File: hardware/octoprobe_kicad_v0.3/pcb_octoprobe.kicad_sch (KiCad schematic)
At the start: 9 parts, among them J102 USB-226-BRW

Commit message: PCB: Oscillator
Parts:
- R104: footprint Resistor_SMD:R_0603_1608Metric -> Resistor_SMD:R_0805_2012Metric
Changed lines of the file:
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@@
 			)
 		)
-		(property "Footprint" "Resistor_SMD:R_0603_1608Metric"
+		(property "Footprint" "Resistor_SMD:R_0805_2012Metric"
 			(at 140.97 46.482 90)
 			(effects

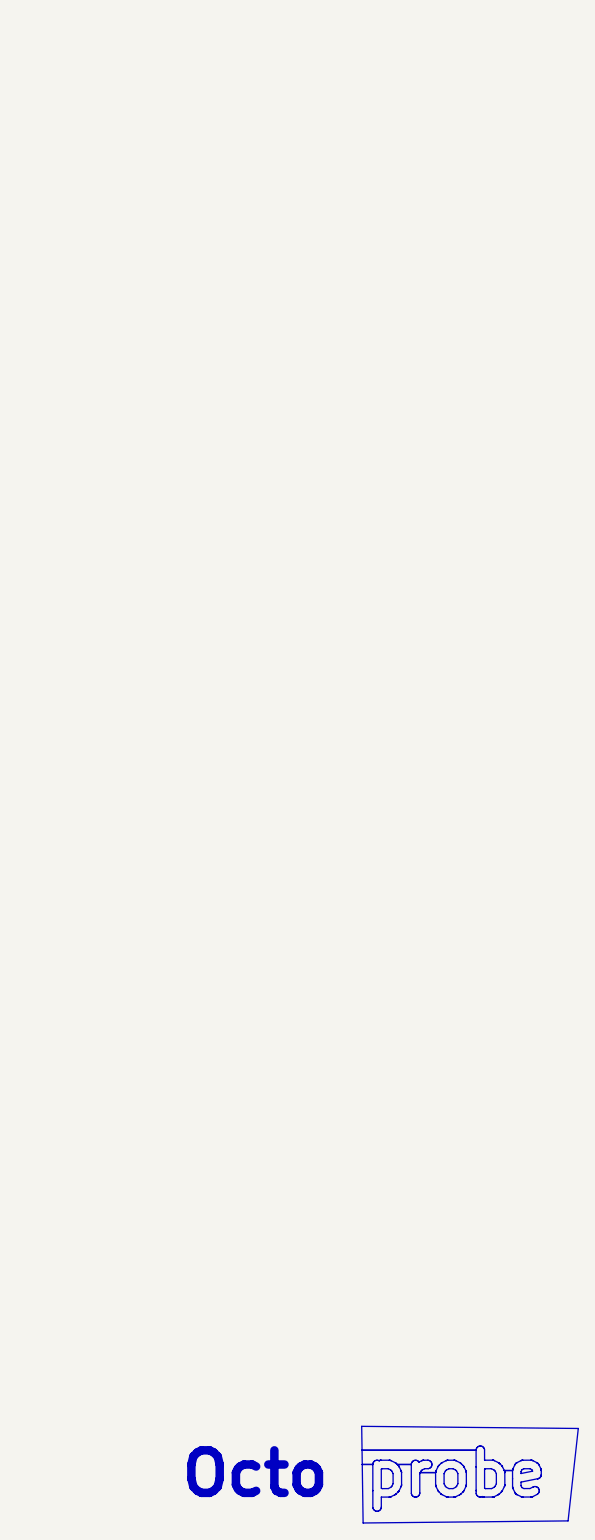
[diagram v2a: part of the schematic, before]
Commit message: PCB: Add "Open Hardware"
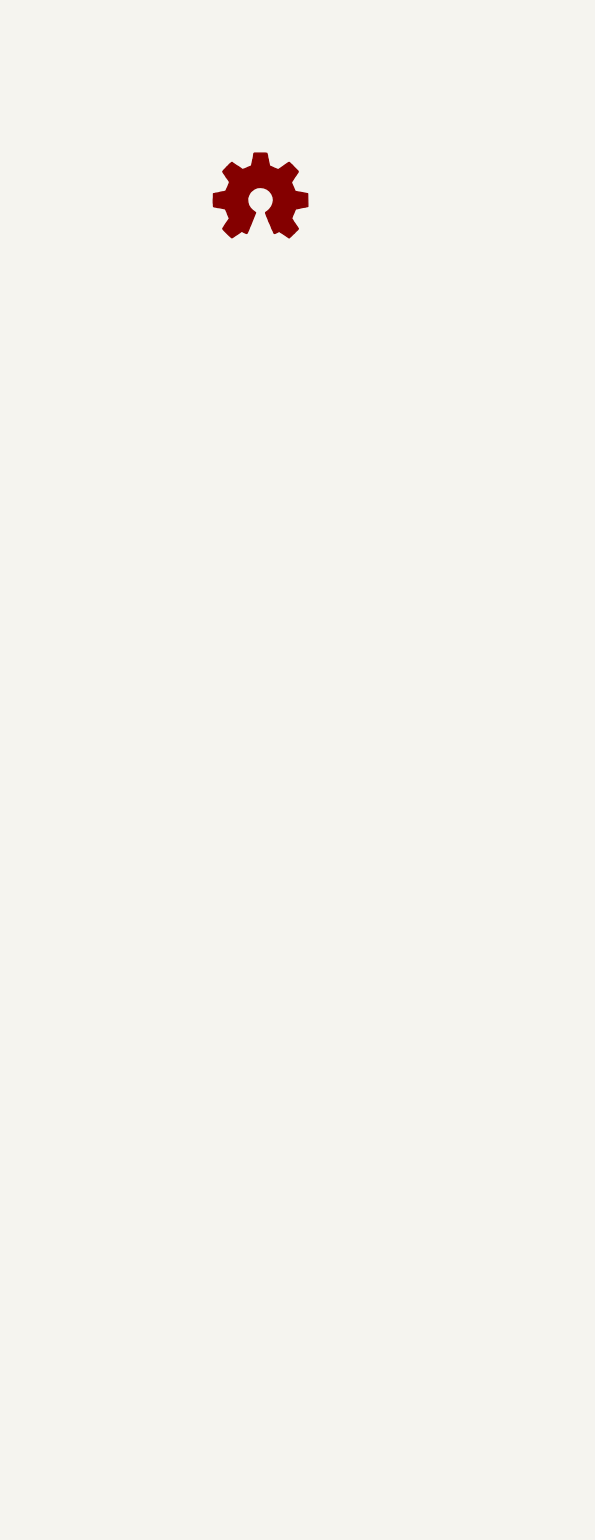
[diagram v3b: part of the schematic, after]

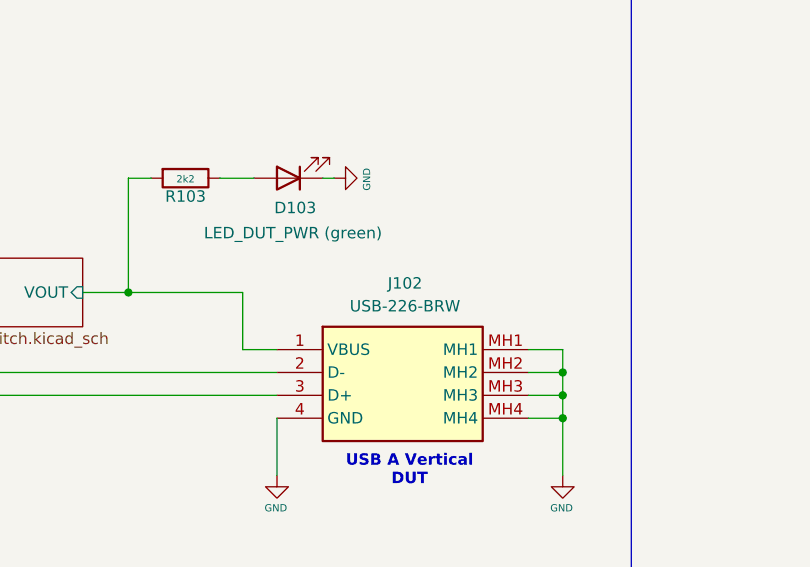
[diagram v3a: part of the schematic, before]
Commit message: PCB: Production files ready
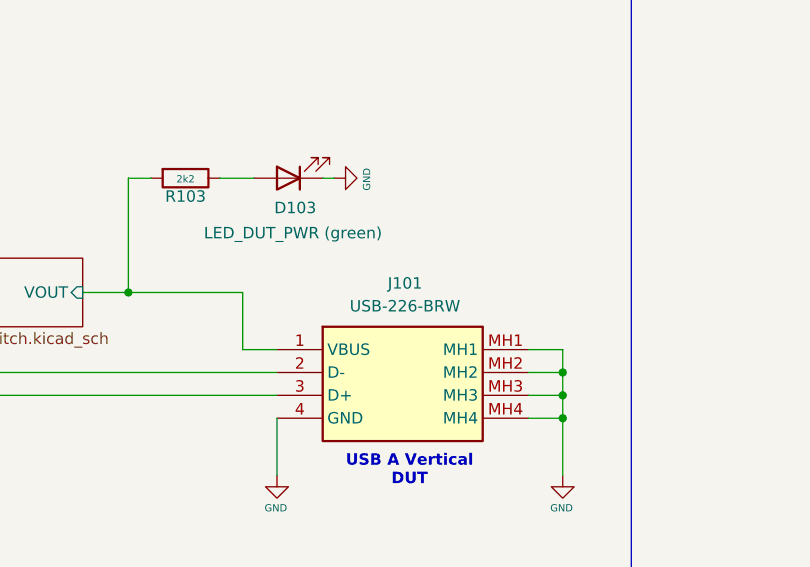
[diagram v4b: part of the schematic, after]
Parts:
- added Logo_open_hardware101: Logo_Open_Hardware_Small, Symbol:OSHW-Logo2_9.8x8mm_SilkScreen, symbol Graphic:Logo_Open_Hardware_Small
- D103, D104: footprint 00_project_library:LED_0603_1608Metric -> LED_SMD:LED_0805_2012Metric
- R102, R103: footprint Resistor_SMD:R_0603_1608Metric -> Resistor_SMD:R_0805_2012Metric
- renumbered J102 to J101
